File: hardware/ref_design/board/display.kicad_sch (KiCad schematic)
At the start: 29 parts, among them J3 FH12-50S-0.5SH(55), Q5 AO3400A, Q6 AO3400A, U6 MCP6002

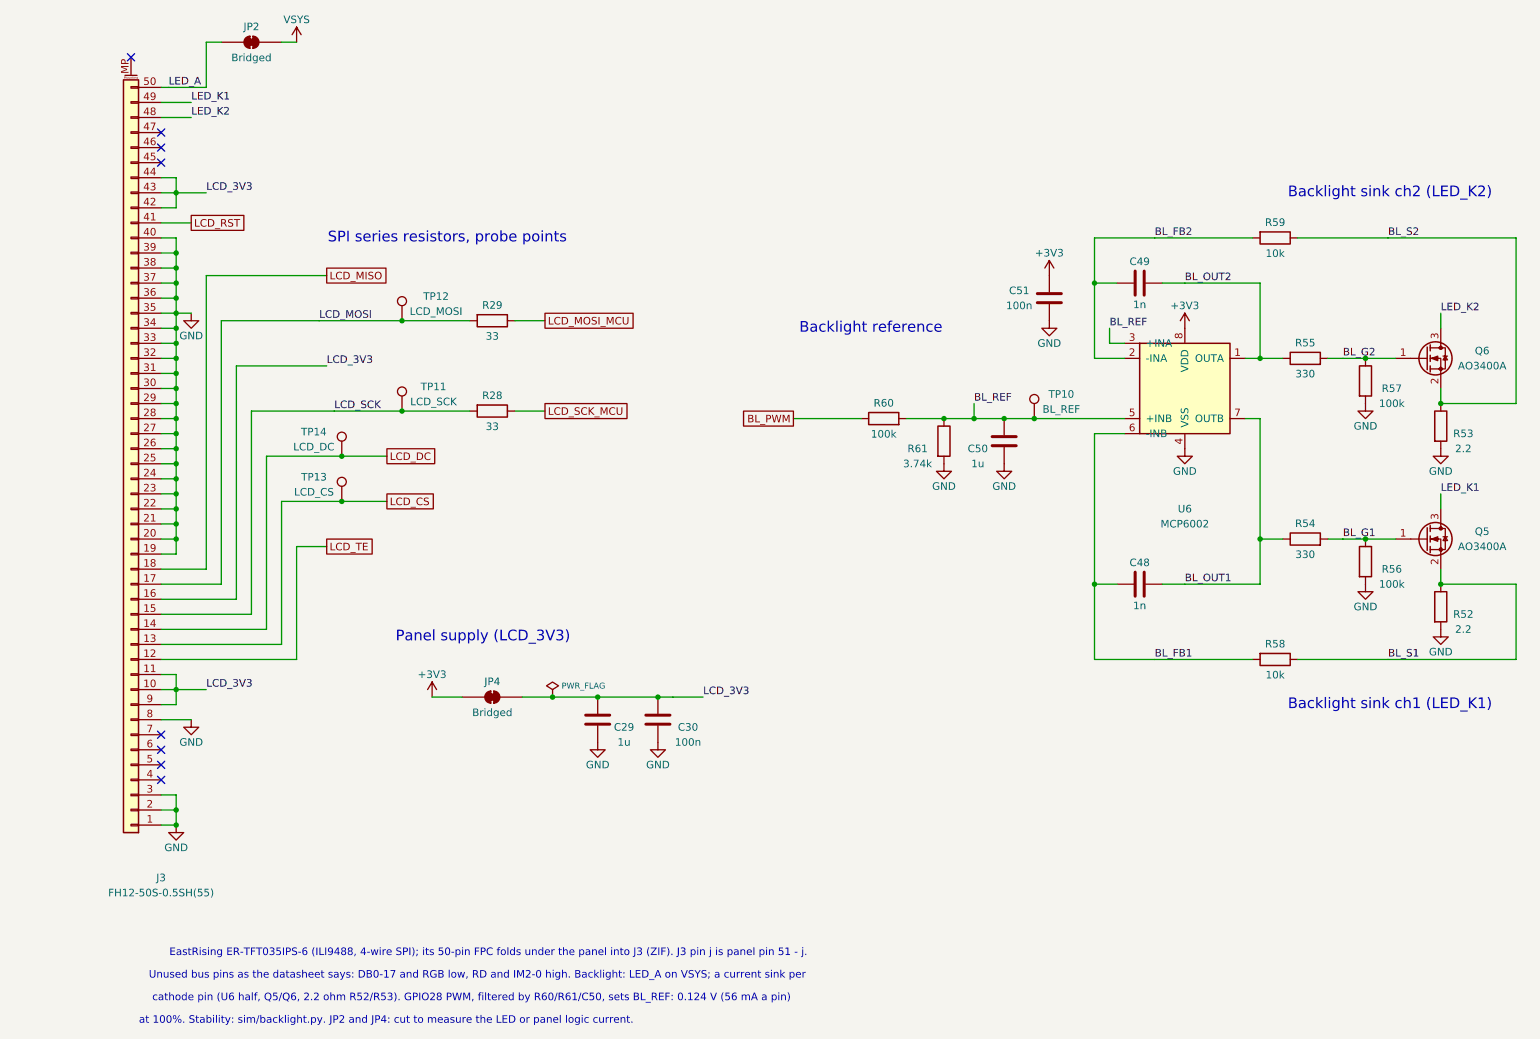
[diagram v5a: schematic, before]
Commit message: ref_design ESP32-S3 schematic: WROOM-1U-N16R8 module, TLV75733P, 8-bit 8080 panel bus (R70-R78), microSD sheet, third 74HC165, BOOT/RESET and J7 pads, 1.5k audio filter; ERC 0, netlist and pin reviews pass
Footprints: battler:ESP32-S3-WROOM-1U (KiCad's without the 0.2 mm thermal vias, tools/fp_esp32.py) and the 4-pad J7. docs/esp32s3_pinmap_diff.md lists the differences from the proposal (no GPIO differs). Unverified: JLC Basic/Extended and stock of the new parts, the DM3AT card-detect pin order.

Co-Authored-By: Claude Sonnet 5.5 <noreply@anthropic.com>
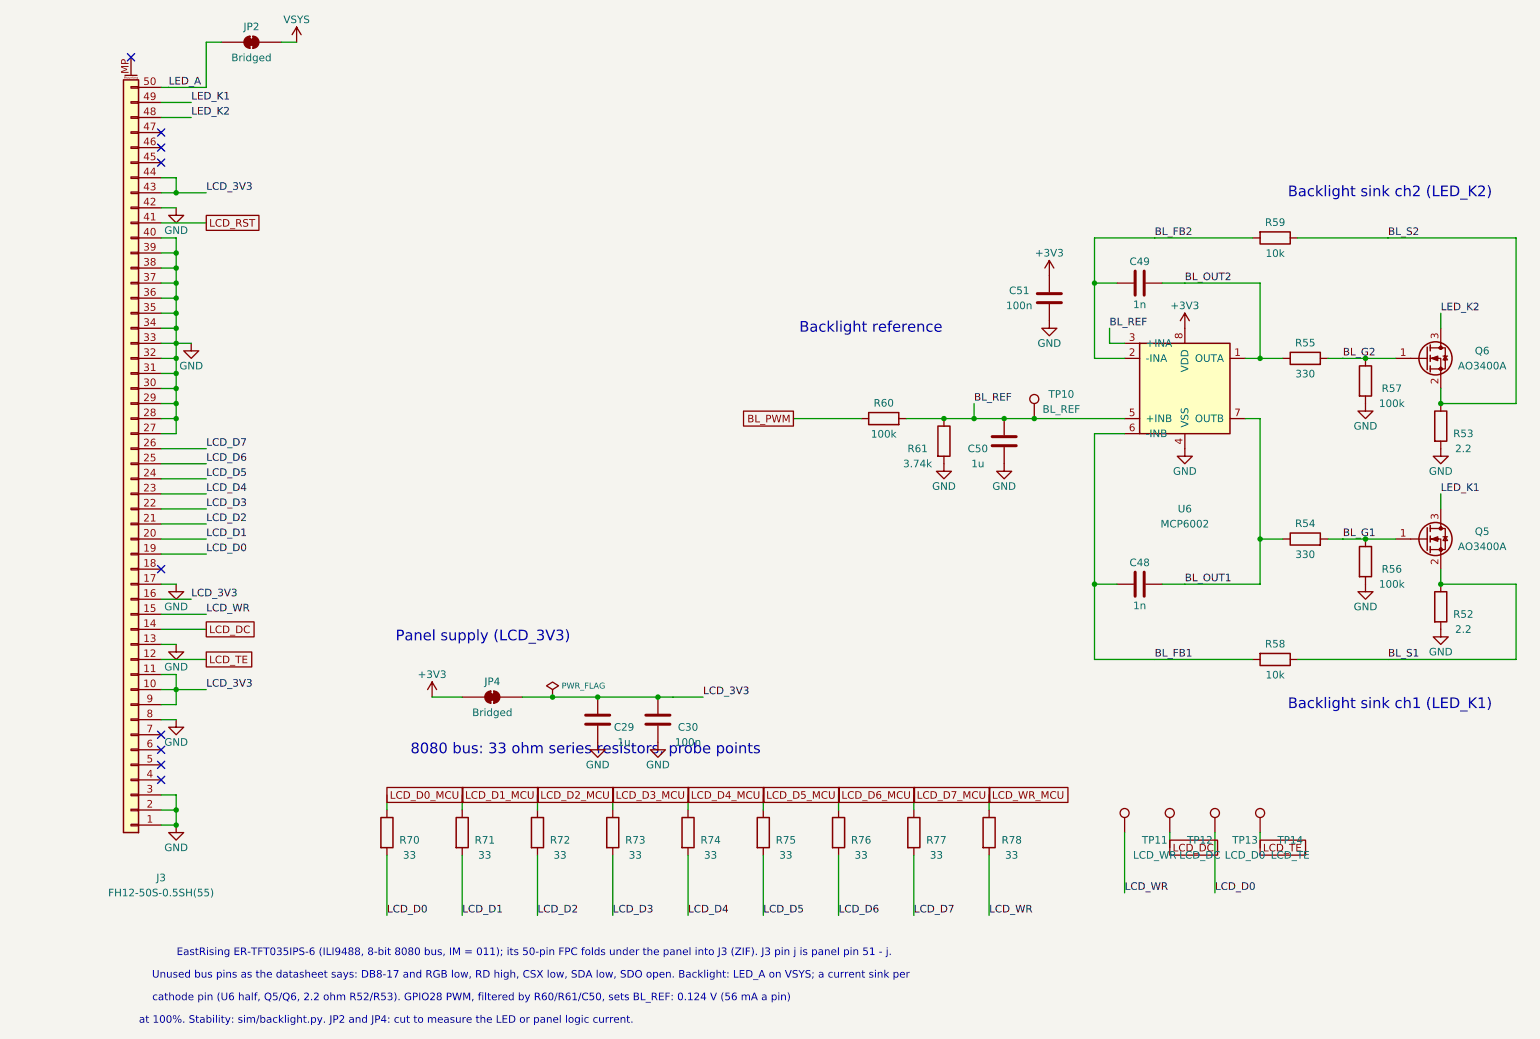
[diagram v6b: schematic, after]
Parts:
- removed R28, R29: 33, Resistor_SMD:R_0402_1005Metric, symbol Device:R
- added R70, R71, R72, R73, R74, R75, R76, R77, R78: 33, Resistor_SMD:R_0402_1005Metric, symbol Device:R
- TP11: value LCD_SCK -> LCD_WR
- TP12: value LCD_MOSI -> LCD_DC
- TP13: value LCD_CS -> LCD_D0
- TP14: value LCD_DC -> LCD_TE
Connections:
- net GND: now also J3.13 (Pin_13), J3.17 (Pin_17), J3.42 (Pin_42); no longer J3.19 (Pin_19), J3.20 (Pin_20), J3.21 (Pin_21), J3.22 (Pin_22), J3.23 (Pin_23), J3.24 (Pin_24), J3.25 (Pin_25), J3.26 (Pin_26)
- net LCD_3V3: no longer J3.42 (Pin_42)
- net LCD_DC: now also TP12.1; no longer TP14.1
- net LCD_TE: now also TP14.1
- net LCD_CS renamed LCD_D0
- net LCD_D0: now also J3.19 (Pin_19), R70.2; no longer J3.13 (Pin_13)
- net LCD_MISO: no longer names the net of J3.18 (Pin_18)
- removed net LCD_MOSI: J3.17 (Pin_17), TP12.1
- net LCD_SCK renamed LCD_WR
- net LCD_WR: now also R78.2
- new net LCD_D0_MCU: R70.1
- new net LCD_D1: J3.20 (Pin_20), R71.2
- new net LCD_D1_MCU: R71.1
- new net LCD_D2: J3.21 (Pin_21), R72.2
- new net LCD_D2_MCU: R72.1
- new net LCD_D3: J3.22 (Pin_22), R73.2
- new net LCD_D3_MCU: R73.1
- new net LCD_D4: J3.23 (Pin_23), R74.2
- new net LCD_D4_MCU: R74.1
- new net LCD_D5: J3.24 (Pin_24), R75.2
- new net LCD_D5_MCU: R75.1
- new net LCD_D6: J3.25 (Pin_25), R76.2
- new net LCD_D6_MCU: R76.1
- new net LCD_D7: J3.26 (Pin_26), R77.2
- new net LCD_D7_MCU: R77.1
- new net LCD_WR_MCU: R78.1
- no-connect marks 8 -> 9
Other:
- note added: "8080 bus: 33 ohm series resistors, probe points"
- note added: "EastRising ER-TFT035IPS-6 (ILI9488, 8-bit 8080 bus, IM = 011); its 50-pin FPC folds under the panel into J3 (ZIF). J3 pin j is panel pin 51 - j."
- note added: "Unused bus pins as the datasheet says: DB8-17 and RGB low, RD high, CSX low, SDA low, SDO open. Backlight: LED_A on VSYS; a current sink per"
- note removed: "EastRising ER-TFT035IPS-6 (ILI9488, 4-wire SPI); its 50-pin FPC folds under the panel into J3 (ZIF). J3 pin j is panel pin 51 - j."
- note removed: "SPI series resistors, probe points"
- note removed: "Unused bus pins as the datasheet says: DB0-17 and RGB low, RD and IM2-0 high. Backlight: LED_A on VSYS; a current sink per"
- moved on the sheet: TP11, TP12, TP13, TP14
